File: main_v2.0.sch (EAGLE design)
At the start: 74 parts, among them IC1 LM321MF, IC2 LM321MF, IC4 LM321MF, U1 BSC076N, U10 IR2101S, U11 TLV73333PDBVT, U2 STM32F030K6T6TR, U3 BSC076N, U4 BSC076N, U5 BSC076N, U6 IR2101S, U7 BSC076N, U8 IR2101S, U9 BSC076N, Y1 8MHz

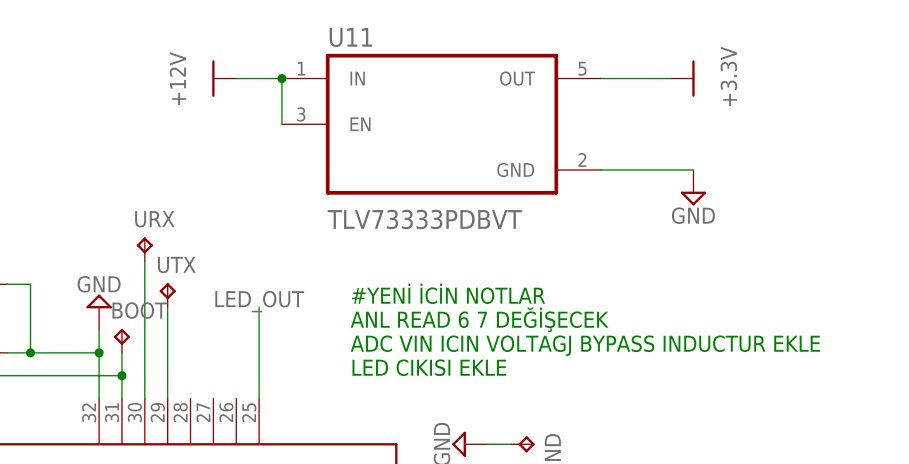
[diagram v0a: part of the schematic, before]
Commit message: updated ldo regulator
we are tested working project
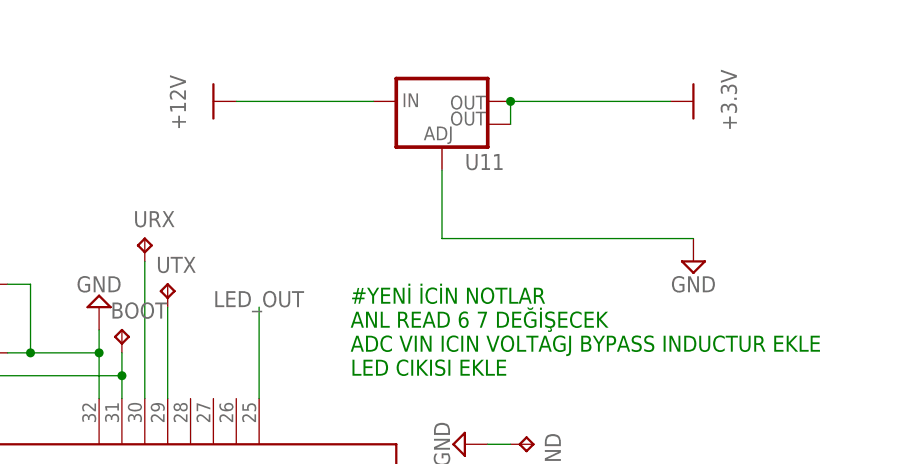
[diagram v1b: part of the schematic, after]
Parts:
- U11: value TLV73333PDBVT -> (none); device TLV73333PDBVT:TLV73333PDBVT -> SparkFun-IC-Power:V_REG_LM1117SOT223
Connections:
- net +12V: no longer U11.EN
- net +3.3V: now also U11.OUT@1
- net GND: now also U11.ADJ; no longer U11.GND
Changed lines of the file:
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@@
 <part name="SUPPLY22" library="Power_Symbols" library_urn="urn:adsk.eagle:library:16502351" deviceset="GND" device="" value="GND"/>
 <part name="SUPPLY23" library="Power_Symbols" library_urn="urn:adsk.eagle:library:16502351" deviceset="+3.3V" device="" value="+3.3V"/>
-<part name="U11" library="TLV73333PDBVT" deviceset="TLV73333PDBVT" device=""/>
 <part name="SUPPLY24" library="Power_Symbols" library_urn="urn:adsk.eagle:library:16502351" deviceset="GND" device="" value="GND"/>
 <part name="SUPPLY25" library="Power_Symbols" library_urn="urn:adsk.eagle:library:16502351" deviceset="GND" device="" value="GND"/>
@@
 <part name="C9" library="Capacitor" library_urn="urn:adsk.eagle:library:16290819" deviceset="C" device="CHIP-0805(2012-METRIC)" package3d_urn="urn:adsk.eagle:package:16290897/2" technology="_" value="100nF"/>
 <part name="C14" library="Capacitor" library_urn="urn:adsk.eagle:library:16290819" deviceset="C" device="CHIP-0805(2012-METRIC)" package3d_urn="urn:adsk.eagle:package:16290897/2" technology="_" value="100nF"/>
+<part name="U11" library="SparkFun-IC-Power" library_urn="urn:adsk.eagle:library:526" deviceset="V_REG_LM1117" device="SOT223" package3d_urn="urn:adsk.eagle:package:39069/1"/>
 </parts>
 <sheets>
@@
 <attribute name="VALUE" x="165.608" y="177.927" size="1.778" layer="96" rot="R270" align="bottom-center"/>
 </instance>
-<instance part="SUPPLY2" gate="G$1" x="167.64" y="246.38" smashed="yes" rot="R270">
-<attribute name="VALUE" x="173.228" y="246.507" size="1.778" layer="96" rot="R270" align="bottom-center"/>
-</instance>
-<instance part="SUPPLY10" gate="G$1" x="170.18" y="233.68" smashed="yes">
-<attribute name="VALUE" x="170.18" y="231.14" size="1.778" layer="96" align="center"/>
-</instance>
-<instance part="SUPPLY11" gate="G$1" x="119.38" y="246.38" smashed="yes" rot="R90">
-<attribute name="VALUE" x="113.792" y="246.253" size="1.778" layer="96" rot="R90" align="bottom-center"/>
+<instance part="SUPPLY2" gate="G$1" x="167.64" y="243.84" smashed="yes" rot="R270">
+<attribute name="VALUE" x="173.228" y="243.967" size="1.778" layer="96" rot="R270" align="bottom-center"/>
+</instance>
+<instance part="SUPPLY10" gate="G$1" x="170.18" y="226.06" smashed="yes">
+<attribute name="VALUE" x="170.18" y="223.52" size="1.778" layer="96" align="center"/>
+</instance>
+<instance part="SUPPLY11" gate="G$1" x="119.38" y="243.84" smashed="yes" rot="R90">
+<attribute name="VALUE" x="113.792" y="243.713" size="1.778" layer="96" rot="R90" align="bottom-center"/>
 </instance>
 <instance part="C6" gate="G$1" x="215.9" y="236.22" smashed="yes">
@@
 <attribute name="VALUE" x="352.933" y="173.228" size="1.778" layer="96" align="bottom-center"/>
 </instance>
-<instance part="U11" gate="G$1" x="142.24" y="241.3" smashed="yes">
-<attribute name="NAME" x="129.54" y="249.92" size="2.0828" layer="95" ratio="10" rot="SR0"/>
-<attribute name="VALUE" x="129.54" y="229.68" size="2.0828" layer="96" ratio="10" rot="SR0"/>
-</instance>
 <instance part="SUPPLY24" gate="G$1" x="327.66" y="137.16" smashed="yes">
 <attribute name="VALUE" x="327.66" y="134.62" size="1.778" layer="96" align="center"/>
@@
 <attribute name="NAME" x="330.2" y="149.86" size="1.778" layer="95"/>
 <attribute name="VALUE" x="330.2" y="147.32" size="1.778" layer="96"/>
+</instance>
+<instance part="U11" gate="G$1" x="142.24" y="243.84" smashed="yes">
+<attribute name="NAME" x="144.78" y="236.22" size="1.778" layer="95" font="vector"/>
+<attribute name="VALUE" x="144.78" y="233.68" size="1.778" layer="96" font="vector"/>
 </instance>
 </instances>
@@
 </segment>
 <segment>
-<pinref part="U11" gate="G$1" pin="GND"/>
 <pinref part="SUPPLY10" gate="G$1" pin="GND"/>
-<wire x1="160.02" y1="236.22" x2="170.18" y2="236.22" width="0.1524" layer="91"/>
+<wire x1="170.18" y1="228.6" x2="142.24" y2="228.6" width="0.1524" layer="91"/>
+<pinref part="U11" gate="G$1" pin="ADJ"/>
+<wire x1="142.24" y1="236.22" x2="142.24" y2="228.6" width="0.1524" layer="91"/>
 </segment>
 <segment>
@@
 </segment>
 <segment>
+<pinref part="SUPPLY2" gate="G$1" pin="+3.3V"/>
+<wire x1="149.86" y1="243.84" x2="167.64" y2="243.84" width="0.1524" layer="91"/>
 <pinref part="U11" gate="G$1" pin="OUT"/>
-<pinref part="SUPPLY2" gate="G$1" pin="+3.3V"/>
-<wire x1="160.02" y1="246.38" x2="167.64" y2="246.38" width="0.1524" layer="91"/>
+<pinref part="U11" gate="G$1" pin="OUT@1"/>
+<wire x1="149.86" y1="241.3" x2="149.86" y2="243.84" width="0.1524" layer="91"/>
+<junction x="149.86" y="243.84"/>
 </segment>
 </net>
@@
 <segment>
 <pinref part="SUPPLY11" gate="G$1" pin="+12V"/>
+<wire x1="134.62" y1="243.84" x2="119.38" y2="243.84" width="0.1524" layer="91"/>
 <pinref part="U11" gate="G$1" pin="IN"/>
-<wire x1="119.38" y1="246.38" x2="124.46" y2="246.38" width="0.1524" layer="91"/>
-<pinref part="U11" gate="G$1" pin="EN"/>
-<wire x1="124.46" y1="241.3" x2="124.46" y2="246.38" width="0.1524" layer="91"/>
-<junction x="124.46" y="246.38"/>
 </segment>
 </net>
